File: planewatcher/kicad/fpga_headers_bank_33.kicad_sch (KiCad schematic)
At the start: 7 parts, among them J4 FPGA BANK 33

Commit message: Populate Z13 with 68nH
After initial testing of the prototype 1.3, Z13 was populated with 68nH which improved RF performance significantly.
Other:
- company: (none) -> plane.watch
- title: (none) -> Plane Watcher
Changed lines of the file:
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@@
 	(paper "A4")
 	(title_block
+		(title "Plane Watcher")
+		(date "2026-09-25")
+		(rev "1.4")
+		(company "plane.watch")
+		(comment 1 "No warranty; see LICENSE.")
 		(comment 2 "Source: https://github.com/plane-watch/hardware.")
 		(comment 3 "Licensed under CERN-OHL-S-2.0.")
@@
 					(reference "C1")
 					(unit 1)
+					(variant
+						(name "revision_1.4")
+					)
 				)
 			)
@@
 					(reference "J4")
 					(unit 1)
+					(variant
+						(name "revision_1.4")
+					)
 				)
 			)
@@
 					(reference "C12")
 					(unit 1)
+					(variant
+						(name "revision_1.4")
+					)
 				)
 			)
@@
 					(reference "C13")
 					(unit 1)
+					(variant
+						(name "revision_1.4")
+					)
 				)
 			)
@@
 					(reference "C14")
 					(unit 1)
+					(variant
+						(name "revision_1.4")
+					)
 				)
 			)
@@
 					(reference "C10")
 					(unit 1)
+					(variant
+						(name "revision_1.4")
+					)
 				)
 			)
@@
 					(reference "C11")
 					(unit 1)
-				)
-			)
+					(variant
+						(name "revision_1.4")
+					)
+				)
+			)

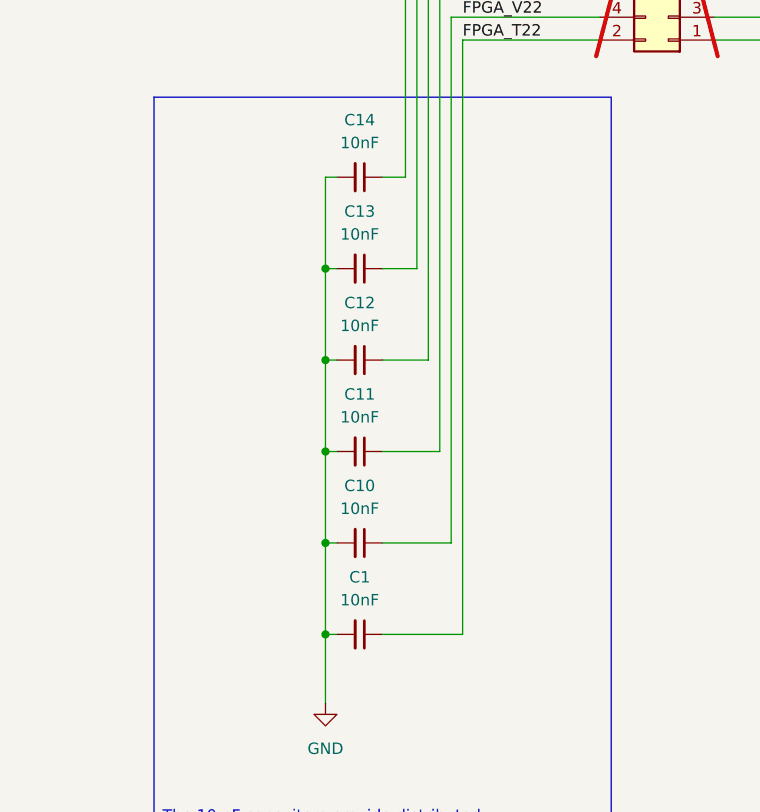
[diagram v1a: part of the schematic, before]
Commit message: Update symbols to Kicad 10.0.5
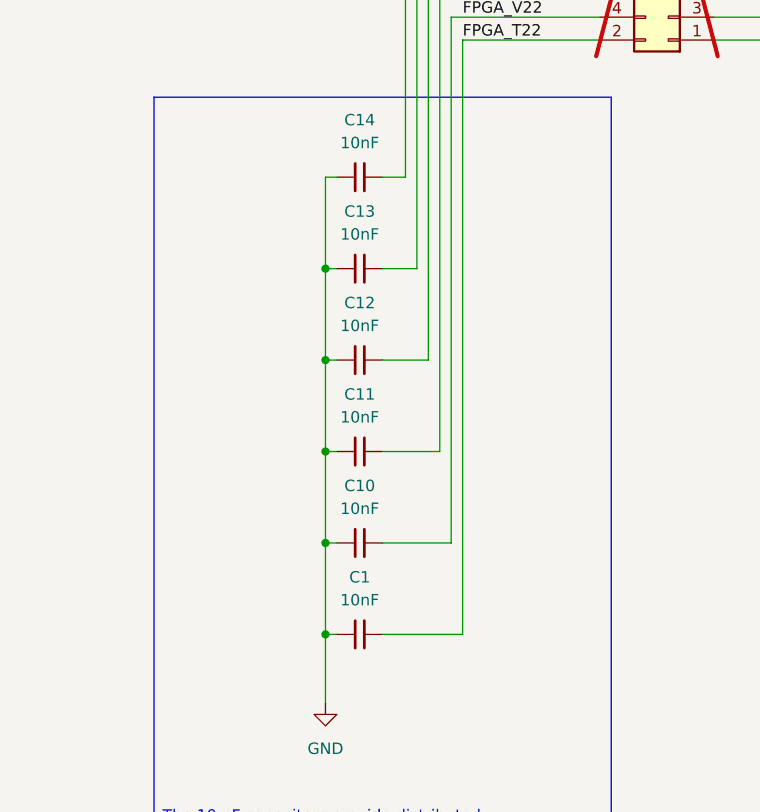
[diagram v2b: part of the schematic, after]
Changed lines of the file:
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@@
 					(reference "C1")
 					(unit 1)
-					(variant
-						(name "revision_1.4")
-					)
 				)
 			)
@@
 					(reference "J4")
 					(unit 1)
-					(variant
-						(name "revision_1.4")
-					)
 				)
 			)
@@
 					(reference "C12")
 					(unit 1)
-					(variant
-						(name "revision_1.4")
-					)
 				)
 			)
@@
 					(reference "C13")
 					(unit 1)
-					(variant
-						(name "revision_1.4")
-					)
 				)
 			)
@@
 					(reference "C14")
 					(unit 1)
-					(variant
-						(name "revision_1.4")
-					)
 				)
 			)
@@
 					(reference "C10")
 					(unit 1)
-					(variant
-						(name "revision_1.4")
-					)
 				)
 			)
@@
 					(reference "C11")
 					(unit 1)
-					(variant
-						(name "revision_1.4")
-					)
-				)
-			)
+				)
+			)

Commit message: Add comments & markup to schematic
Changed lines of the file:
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@@
 		)
 	)
-	(text_box "The 10 nF capacitors provide distributed, low-impedance high-frequency return paths from the board ground to spare FPGA pins driven low, reducing return-loop area and associated noise."
+	(text_box "On the first prototype (1.2), we had some issues with noise triggering low bits on the ADC output. These caps were added in an effort to try and squash that noise.\n\n\"The 10 nF capacitors provide distributed, low-impedance high-frequency return paths from the board ground to spare FPGA pins driven low, reducing return-loop area and associated noise.\""
 		(exclude_from_sim no)
 		(at 92.71 81.28 0)
-		(size 50.8 87.63)
+		(size 50.8 99.06)
 		(margins 0.9525 0.9525 0.9525 0.9525)
 		(stroke
